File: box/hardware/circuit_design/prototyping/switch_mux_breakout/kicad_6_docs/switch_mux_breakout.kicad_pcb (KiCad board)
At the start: 2 copper layers, 52.1 x 61 mm, 18 parts, among them J1 rpi_port, SW1 SW_DIP_x08, SW2 SW_DIP_x08, SW3 SW_DIP_x08, SW4 SW_DIP_x08, U1 MCP23S18T-E/SO, U2 MCP23S18T-E/SO

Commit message: Update switches to use I2C instead of SPI
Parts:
- added JP2: SolderJumper_3_Open, Jumper:SolderJumper-3_P1.3mm_Open_Pad1.0x1.5mm, F.Cu at (113.3, 99.8)
- added JP3: SolderJumper_3_Open, Jumper:SolderJumper-3_P1.3mm_Open_Pad1.0x1.5mm, F.Cu at (116.5, 99.8)
- added JP4: SolderJumper_3_Open, Jumper:SolderJumper-3_P1.3mm_Open_Pad1.0x1.5mm, F.Cu at (119.7, 99.8)
- added JP5: SolderJumper_3_Open, Jumper:SolderJumper-3_P1.3mm_Open_Pad1.0x1.5mm, F.Cu at (113.3, 107.4)
- added JP6: SolderJumper_3_Open, Jumper:SolderJumper-3_P1.3mm_Open_Pad1.0x1.5mm, F.Cu at (116.5, 107.4)
- added JP7: SolderJumper_3_Open, Jumper:SolderJumper-3_P1.3mm_Open_Pad1.0x1.5mm, F.Cu at (119.7, 107.4)
- added R2: 10k, Resistor_SMD:R_0805_2012Metric, F.Cu at (115.6, 87.6)
- added R3: 10k, Resistor_SMD:R_0805_2012Metric, F.Cu at (115.5, 90.2)
- added R4: 10k, Resistor_SMD:R_0805_2012Metric, F.Cu at (115.5, 92.7)
- J1: footprint Connector_PinHeader_2.54mm:PinHeader_1x12_P2.54mm_Vertical -> Connector_PinHeader_2.54mm:PinHeader_1x06_P2.54mm_Vertical
- U1, U2: value MCP23S18T-E/SO -> PCA9555D; footprint Package_SO:SOIC-28W_7.5x17.9mm_P1.27mm -> Package_SO:SOIC-24W_7.5x15.4mm_P1.27mm
- moved R1 34.2 mm to (115.6, 85.1), turned to 180 degrees
- moved C3 22.6 mm to (132.0, 89.4)
- moved C2 22.2 mm to (126.3, 61.9), turned to 90 degrees
- moved D1 15.6 mm to (122.3, 115.2)
- moved R5 13.4 mm to (124.8, 115.2)
- moved U1 1.27 mm to (128.3, 72.4)
- moved U2 1.27 mm to (128.3, 99.1)
- moved C1 1.05 mm to (123.6, 61.9), turned to 90 degrees
- renumbered R2 to R5
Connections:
- J1 pad 2: /SPI.MOSI -> /SCL
- J1 pad 3: /SPI.MISO -> /SDA
- J1 pad 4: /SPI.SCLK -> /~{INT 0-15}
- J1 pad 5: /SPI.CS0 -> /~{INT 16-31}
- J1 pad 6: /SPI.CS1 -> GND
- R1 pad 2: /~{RESET} -> /~{INT 0-15}
- U1 pad 1: GND -> /~{INT 0-15}
- U1 pad 10: /SW7 -> /SW6
- U1 pad 11: +3V3 -> /SW7
- U1 pad 12: /SPI.CS0 -> GND
- U1 pad 13: /SPI.SCLK -> /SW8
- U1 pad 14: /SPI.MOSI -> /SW9
- U1 pad 15: /SPI.MISO -> /SW10
- U1 pad 16: /~{RESET} -> /SW11
- U1 pad 17: unconnected-(U1-Pad17) -> /SW12
- U1 pad 18: /INTB_U1 -> /SW13
- U1 pad 19: /INTA_U1 -> /SW14
- U1 pad 2: unconnected-(U1-Pad2) -> /A1 0-15
- U1 pad 20: /SW8 -> /SW15
- U1 pad 21: /SW9 -> /A0 0-15
- U1 pad 22: /SW10 -> /SCL
- U1 pad 23: /SW11 -> /SDA
- U1 pad 24: /SW12 -> +3V3
- U1 pad 3: /SW0 -> /A2 0-15
- U1 pad 4: /SW1 -> /SW0
- U1 pad 5: /SW2 -> /SW1
- U1 pad 6: /SW3 -> /SW2
- U1 pad 7: /SW4 -> /SW3
- U1 pad 8: /SW5 -> /SW4
- U1 pad 9: /SW6 -> /SW5
- U2 pad 1: GND -> /~{INT 16-31}
- U2 pad 10: /SW23 -> /SW22
- U2 pad 11: +3V3 -> /SW23
- U2 pad 12: /SPI.CS1 -> GND
- U2 pad 13: /SPI.SCLK -> /SW24
- U2 pad 14: /SPI.MOSI -> /SW25
- U2 pad 15: /SPI.MISO -> /SW26
- U2 pad 16: /~{RESET} -> /SW27
- U2 pad 17: unconnected-(U2-Pad17) -> /SW28
- U2 pad 18: /INTB_U2 -> /SW29
- U2 pad 19: /INTA_U2 -> /SW30
- U2 pad 2: unconnected-(U2-Pad2) -> /A1 16-31
- U2 pad 20: /SW24 -> /SW31
- U2 pad 21: /SW25 -> /A0 16-31
- U2 pad 22: /SW26 -> /SCL
- U2 pad 23: /SW27 -> /SDA
- U2 pad 24: /SW28 -> +3V3
- U2 pad 3: /SW16 -> /A2 16-31
- U2 pad 4: /SW17 -> /SW16
- U2 pad 5: /SW18 -> /SW17
- U2 pad 6: /SW19 -> /SW18
- U2 pad 7: /SW20 -> /SW19
- U2 pad 8: /SW21 -> /SW20
- U2 pad 9: /SW22 -> /SW21
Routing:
- net /SDA: track 0.00 -> 80.2 mm, vias 0 -> 1
- net /SCL: track 0.00 -> 76.2 mm, vias 0 -> 1
- net /SPI.MOSI: track 63.8 -> 0.00 mm
- net /~{RESET}: track 59.9 -> 0.00 mm, vias 2 -> 0
- net /SPI.MISO: track 59.8 -> 0.00 mm, vias 2 -> 0
- net /SPI.SCLK: track 49.5 -> 0.00 mm
- net /A0 0-15: track 0.00 -> 40.7 mm, vias 0 -> 2
- net /A1 0-15: track 0.00 -> 37.7 mm, vias 0 -> 2
- net /INTB_U2: track 36.2 -> 0.00 mm, vias 1 -> 0
- net /A2 0-15: track 0.00 -> 35.6 mm
- net /INTA_U2: track 35.4 -> 0.00 mm, vias 1 -> 0
- net /INTA_U1: track 35.2 -> 0.00 mm, vias 1 -> 0
- net +3V3: track 124.1 -> 157.9 mm
- net /A0 16-31: track 0.00 -> 31.7 mm, vias 0 -> 2
- net /SPI.CS1: track 30.7 -> 0.00 mm
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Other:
- board text added: "ADDR 0-15"
- board text added: "ADDR 16-31"
- board text added: "I2C Switch DEMUX eval board rev 0"
- board text added: "PCA9555D"
- board text added: "SCL"
- board text added: "SDA"
- board text added: "active mode"
- board text added: "~{INT0}"
- board text added: "~{INT1}"
- board text removed: "CS0"
- board text removed: "CS1"
- board text removed: "INTA U1"
- board text removed: "INTA U2"
- board text removed: "INTB U1"
- board text removed: "INTB U2"
- board text removed: "MCP23S18-T-E/SO"
- board text removed: "MISO"
- board text removed: "MOSI"
- board text removed: "SCK"
- board text removed: "SPI Switch DEMUX eval board rev 0"
- board text removed: "~{RESET}"

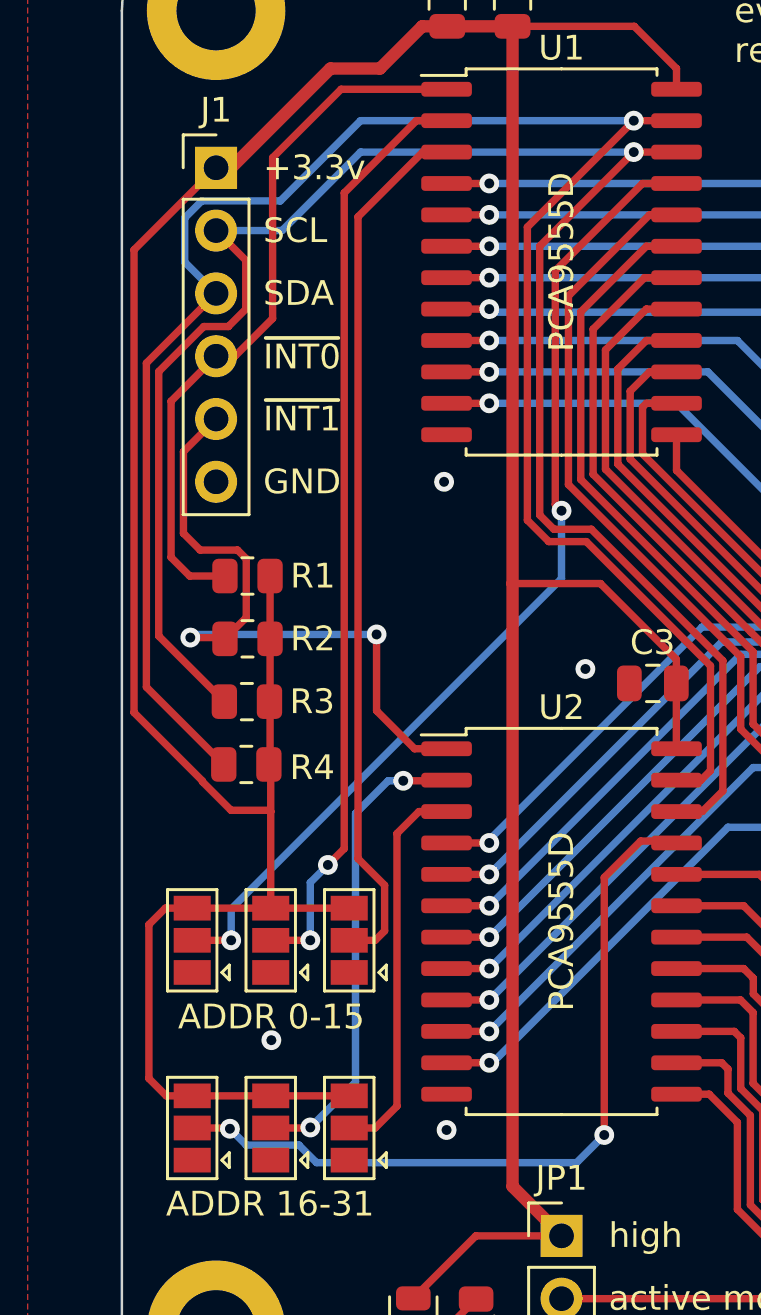
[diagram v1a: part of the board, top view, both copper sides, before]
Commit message: Make I2C address jumpers MSB first
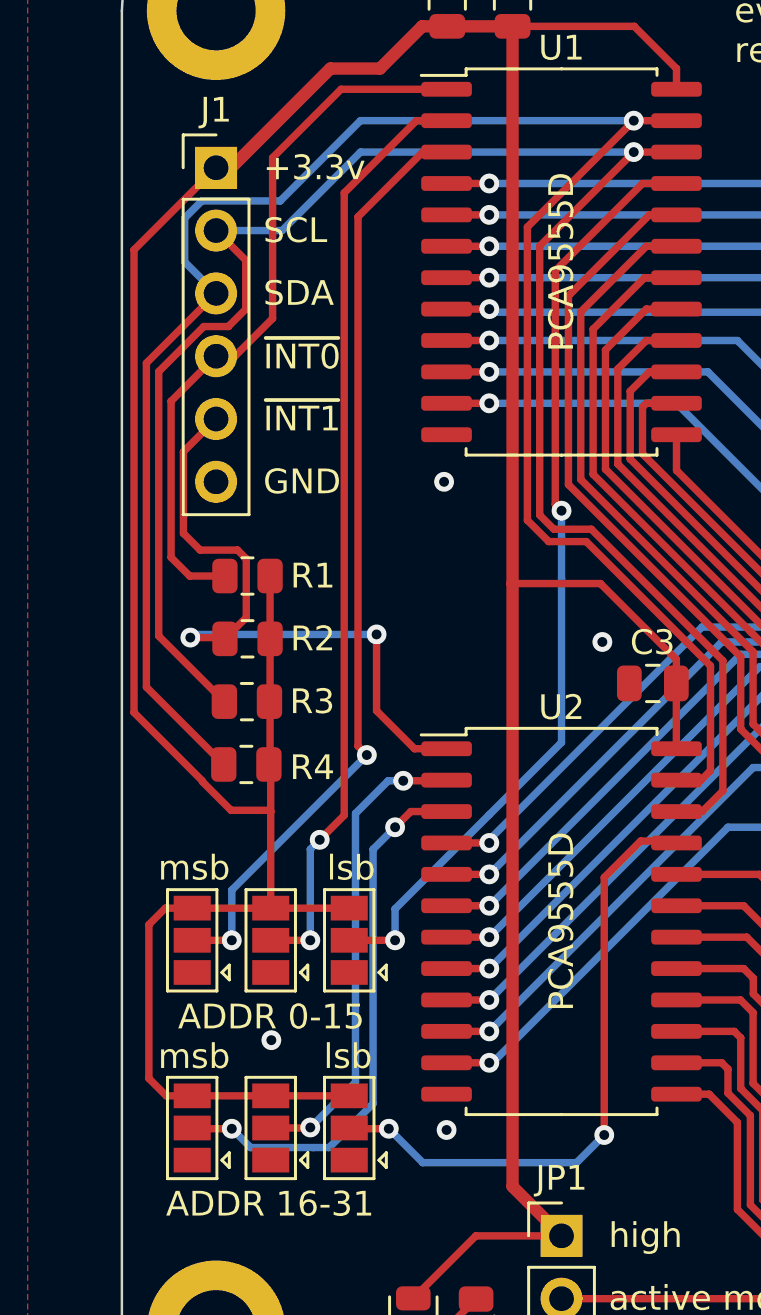
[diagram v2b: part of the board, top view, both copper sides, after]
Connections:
- JP2 pad 2: /A0 0-15 -> /A2 0-15
- JP4 pad 2: /A2 0-15 -> /A0 0-15
- JP5 pad 2: /A0 16-31 -> /A2 16-31
- JP7 pad 2: /A2 16-31 -> /A0 16-31
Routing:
- net /A2 16-31: track 15.7 -> 22.3 mm, vias 0 -> 2
- net /A0 16-31: track 31.7 -> 25.3 mm
- net /A0 0-15: track 40.7 -> 38.2 mm
- net /A2 0-15: track 35.6 -> 37.9 mm, vias 0 -> 2
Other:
- board text added: "lsb"
- board text added: "msb"

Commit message: Change LED and switch breakouts, use headers instead of components
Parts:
- removed JP1: switch_active_hi_lo, Connector_PinHeader_2.54mm:PinHeader_1x03_P2.54mm_Vertical
- removed SW1, SW2, SW3, SW4: SW_DIP_x08, Button_Switch_THT:SW_DIP_SPSTx08_Slide_9.78x22.5mm_W7.62mm_P2.54mm
- added J2: LED_header, Connector_PinHeader_2.54mm:PinHeader_2x20_P2.54mm_Vertical, F.Cu at (148.6, 64.8)
- moved REF** 2.54 mm to (158.8, 59.7)
- moved REF** 2.54 mm to (114.3, 59.7)
- moved REF** 1.27 mm to (158.8, 116.8)
- moved REF** 1.27 mm to (114.3, 116.8)
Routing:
- net Net-(JP1-Pad2): track 129.4 -> 0.00 mm
- net +3V3: track 157.9 -> 202.3 mm
- net /SW0: track 17.6 -> 25.8 mm, vias 1 -> 2
- net /SW1: track 17.3 -> 25.3 mm, vias 1 -> 2
- net /SW3: track 18.4 -> 25.8 mm, vias 1 -> 2
- net /SW4: track 18.9 -> 26.3 mm, vias 1 -> 2
- net /SW6: track 19.9 -> 27.3 mm, vias 1 -> 2
- net /SW5: track 19.4 -> 26.8 mm, vias 1 -> 2
- net /SW2: track 17.8 -> 25.2 mm, vias 1 -> 2
- net /SW7: track 20.5 -> 27.9 mm, vias 1 -> 2
- net /SW8: track 15.4 -> 22.0 mm
- net /SW9: track 21.1 -> 26.6 mm
- net /SW18: track 45.1 -> 39.6 mm
- net /SW19: track 43.5 -> 38.4 mm
- net /SW17: track 45.8 -> 40.9 mm
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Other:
- board size 52.1 x 61 mm -> 52.1 x 64.8 mm
- board text added: "I2C Switch DEMUX rev 0 2022-06-02"
- board text added: "SW 0"
- board text added: "SW 1"
- board text added: "SW 10"
- board text added: "SW 11"
- board text added: "SW 12"
- board text added: "SW 13"
- board text added: "SW 14"
- board text added: "SW 15"
- board text added: "SW 16"
- board text added: "SW 17"
- board text added: "SW 18"
- board text added: "SW 19"
- board text added: "SW 2"
- board text added: "SW 20"
- board text added: "SW 21"
- board text added: "SW 22"
- board text added: "SW 23"
- board text added: "SW 24"
- board text added: "SW 25"
- board text added: "SW 26"
- board text added: "SW 27"
- board text added: "SW 28"
- board text added: "SW 29"
- board text added: "SW 3"
- board text added: "SW 30"
- board text added: "SW 31"
- board text added: "SW 4"
- board text added: "SW 5"
- board text added: "SW 6"
- board text added: "SW 7"
- board text added: "SW 8"
- board text added: "SW 9"
- board text removed: "I2C Switch DEMUX eval board rev 0"
- board text removed: "Set jumper to 'high' to connect switches to +3.3v. Set jumper to 'low' to connect switches to ground."
- board text removed: "active mode"
- board text removed: "high"
- board text removed: "low"
